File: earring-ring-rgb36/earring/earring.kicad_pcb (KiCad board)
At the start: 2 copper layers, 25 x 27.3 mm, 57 parts, among them J1 Conn_01x04, Q1 AO3401A, SW1 SW_Push, U2 STM32L031G6Ux

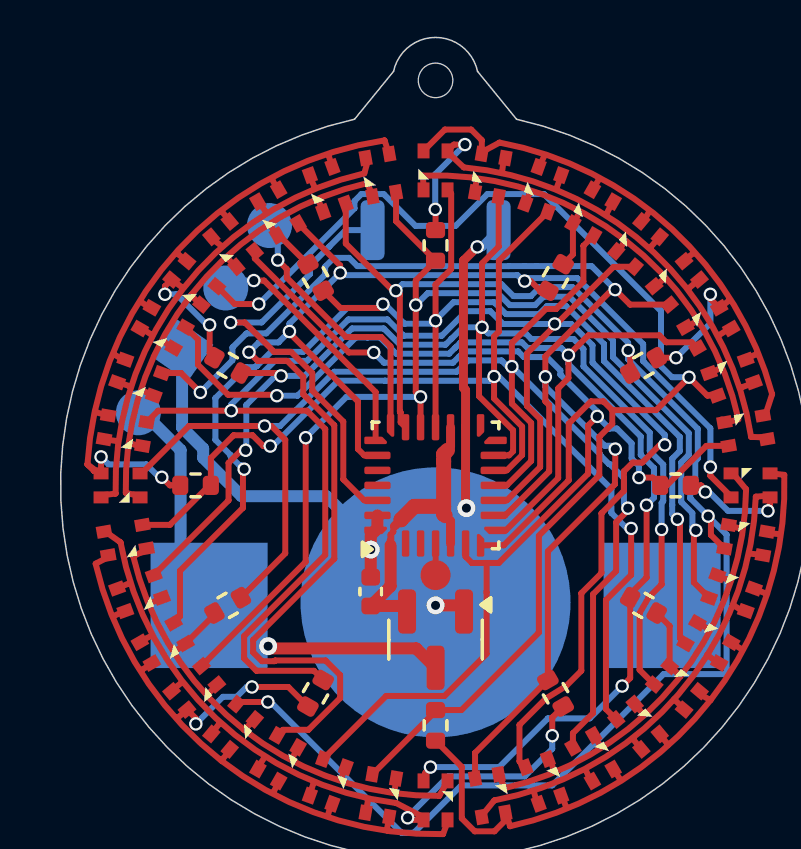
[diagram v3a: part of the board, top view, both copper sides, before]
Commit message: earring-ring-rgb36: added reset pin to programming pins on the side
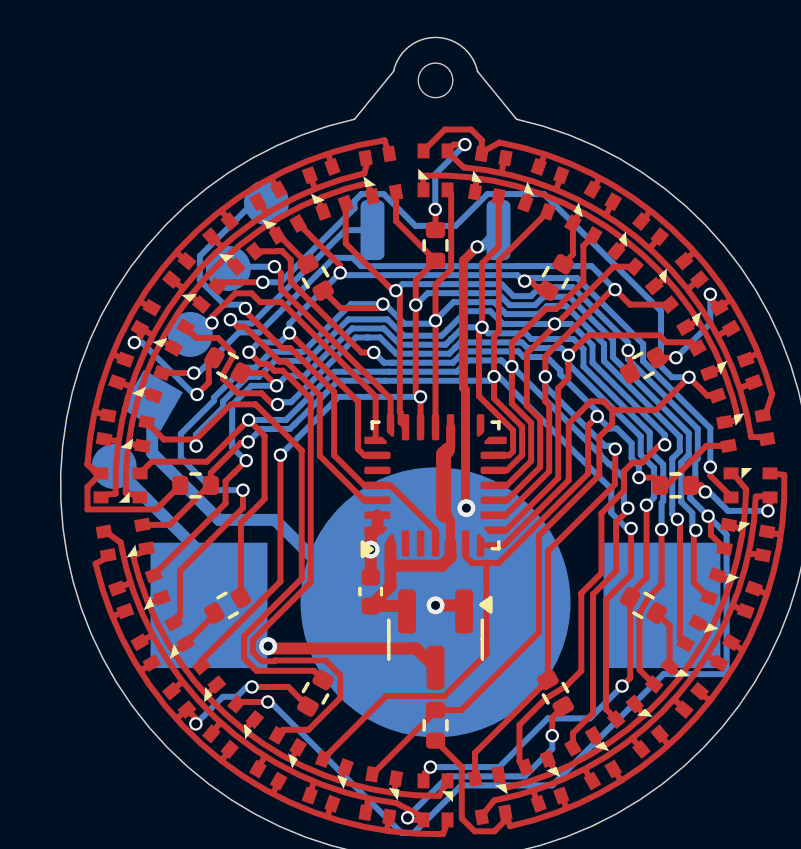
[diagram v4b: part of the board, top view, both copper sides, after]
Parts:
- removed TP1: TestPoint_Small, Custom:TestPoint_1.0x1.0mm
- J1: value Conn_01x04 -> Conn_01x05
- moved J1 1.94 mm to (-8.81, -3.93), turned to 60 degrees
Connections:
- U2 pad 25: unconnected-(U2-PB6-Pad25) -> NRST
- U2 pad 4: Net-(U2-NRST) -> NRST
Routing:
- net NRST: track 0.00 -> 16.8 mm, vias 0 -> 1
- net VBAT: track 15.7 -> 14.1 mm
- net A4: track 46.3 -> 47.8 mm
- net SWCLK: track 8.25 -> 9.75 mm
- net A8: track 60.1 -> 61.6 mm
- net A6R: track 3.98 -> 5.21 mm, vias 2 -> 0
- net A5R: track 3.66 -> 4.82 mm
- net Net-(U2-NRST): track 0.99 -> 0.00 mm
- net A1: track 50.0 -> 49.1 mm
- net A9: track 46.1 -> 45.2 mm
- net A6: track 39.0 -> 38.4 mm
- net A5: track 43.6 -> 44.2 mm
- net SWDIO: track 9.02 -> 8.46 mm
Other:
- board text added: "RST"

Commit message: earring-ring-rgb36: update PCB for production
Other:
- board text added: "CR1225"
- board text added: "LED earring"
- board text added: "v1.0"
- board text removed: "LED earring v0.3"
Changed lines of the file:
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@@
 		)
 		(embedded_fonts no)
-		(model "${KICAD8_3DMODEL_DIR}/Button_Switch_SMD.3dshapes/SW_Push_SPST_NO_Alps_SKRK.wrl"
+		(model "${KICAD9_3DMODEL_DIR}/Button_Switch_SMD.3dshapes/SW_SPST_B3U-1000P-B.wrl"
 			(offset
 				(xyz 0 0 0)
@@
 		)
 		(embedded_fonts no)
+		(model "${KICAD9_3DMODEL_DIR}/Battery.3dshapes/Battery_CR1225.wrl"
+			(offset
+				(xyz 0 0 0)
+			)
+			(scale
+				(xyz 1 1 1)
+			)
+			(rotate
+				(xyz -0 -0 -0)
+			)
+		)
 	)
 	(gr_line
@@
 		)
 	)
-	(gr_text "LED earring\nv0.3"
-		(at 0 -3.4 0)
+	(gr_text "LED earring"
+		(at 0 -4.2 0)
 		(layer "B.SilkS")
 		(effects
@@
 		)
 	)
+	(gr_text "CR1225"
+		(at 0 11.5 0)
+		(layer "B.SilkS")
+		(effects
+			(font
+				(size 1.5 1.5)
+				(thickness 0.25)
+				(bold yes)
+			)
+			(justify bottom mirror)
+		)
+	)
 	(gr_text "RST\n"
 		(at -3.44 -7.64 330)
@@
 			)
 			(justify left bottom mirror)
+		)
+	)
+	(gr_text "v1.0"
+		(at 5 0.6 315)
+		(layer "B.SilkS")
+		(effects
+			(font
+				(size 1 1)
+				(thickness 0.153)
+			)
+			(justify left bottom mirror)

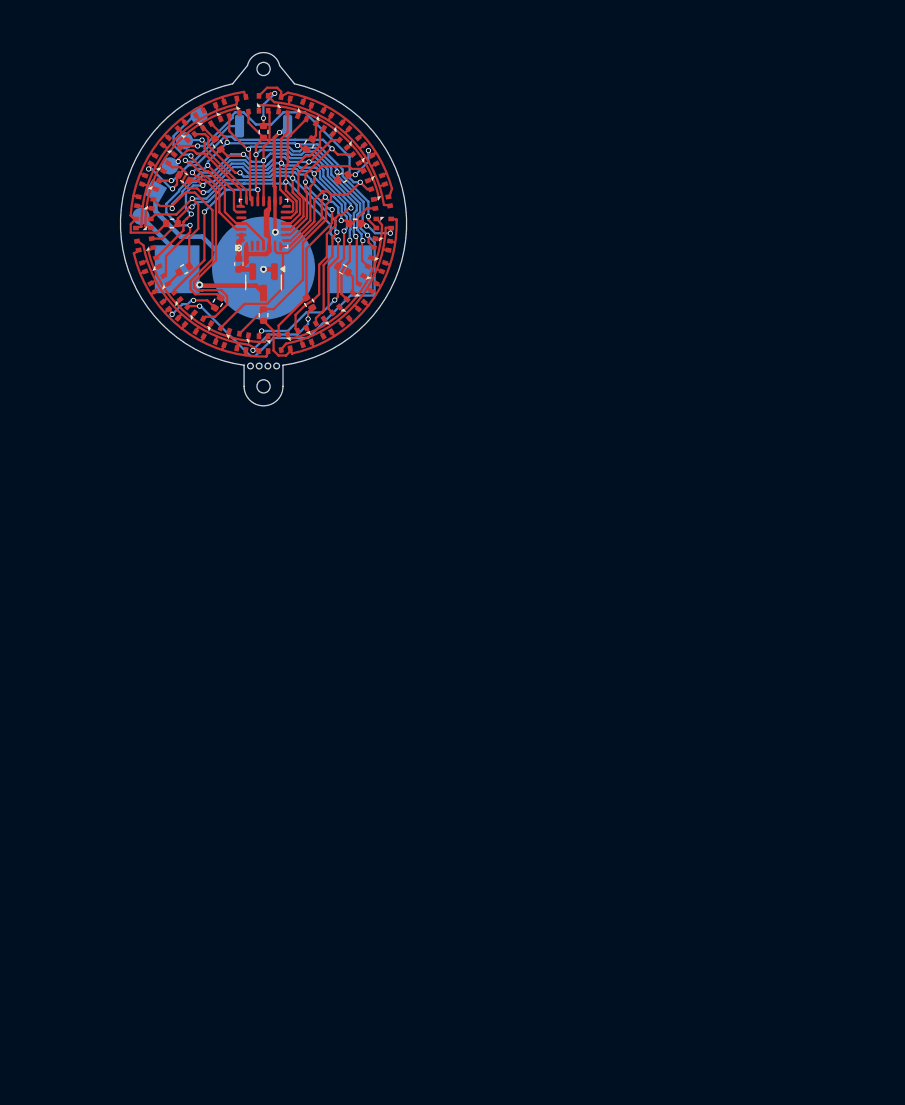
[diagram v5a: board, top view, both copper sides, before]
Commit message: earring-ring-rgb36: panelize PCB
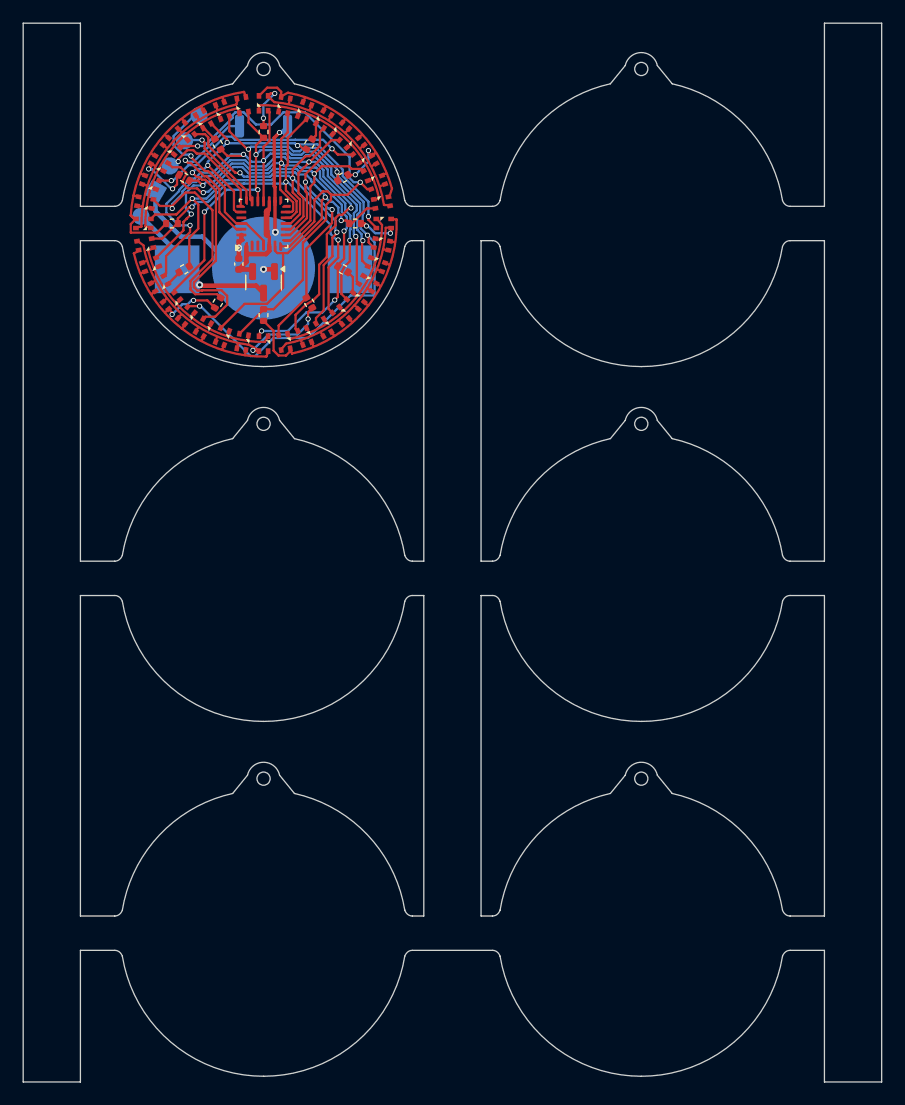
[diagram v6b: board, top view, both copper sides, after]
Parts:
- removed H2: ToolingHole, Custom:ToolingHoleWithMouseBytes
- added H1: ToolingHole, Custom:ToolingHole_JLCPCB, F.Cu at (33.0, -13.5)
- added H1: ToolingHole, Custom:ToolingHole_JLCPCB, F.Cu at (0.00, 17.5)
- added H1: ToolingHole, Custom:ToolingHole_JLCPCB, F.Cu at (33.0, 48.5)
- added H1: ToolingHole, Custom:ToolingHole_JLCPCB, F.Cu at (33.0, 17.5)
- added H1: ToolingHole, Custom:ToolingHole_JLCPCB, F.Cu at (0.00, 48.5)
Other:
- board size 25 x 27.3 mm -> 75 x 92.5 mm
- board text added: "V-cut"
